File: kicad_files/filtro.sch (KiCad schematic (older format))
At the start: 16 parts

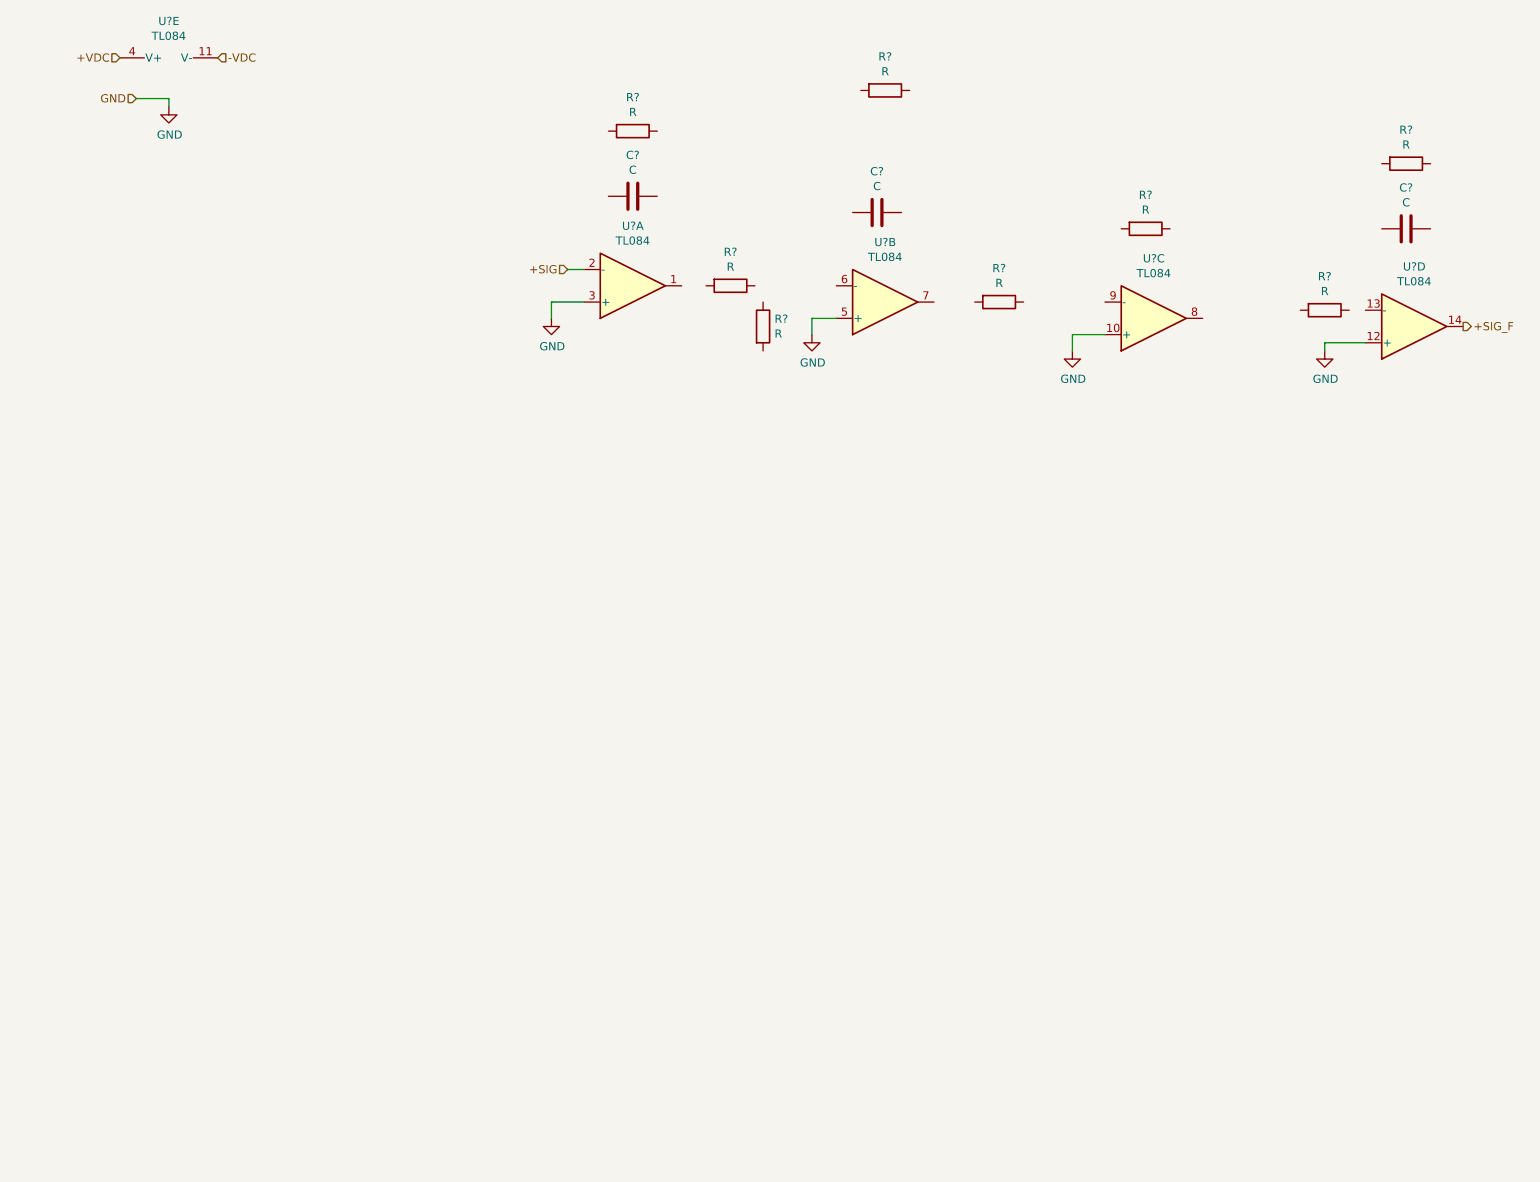
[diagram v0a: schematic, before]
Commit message: Esquemático do filtro conectado e revisado
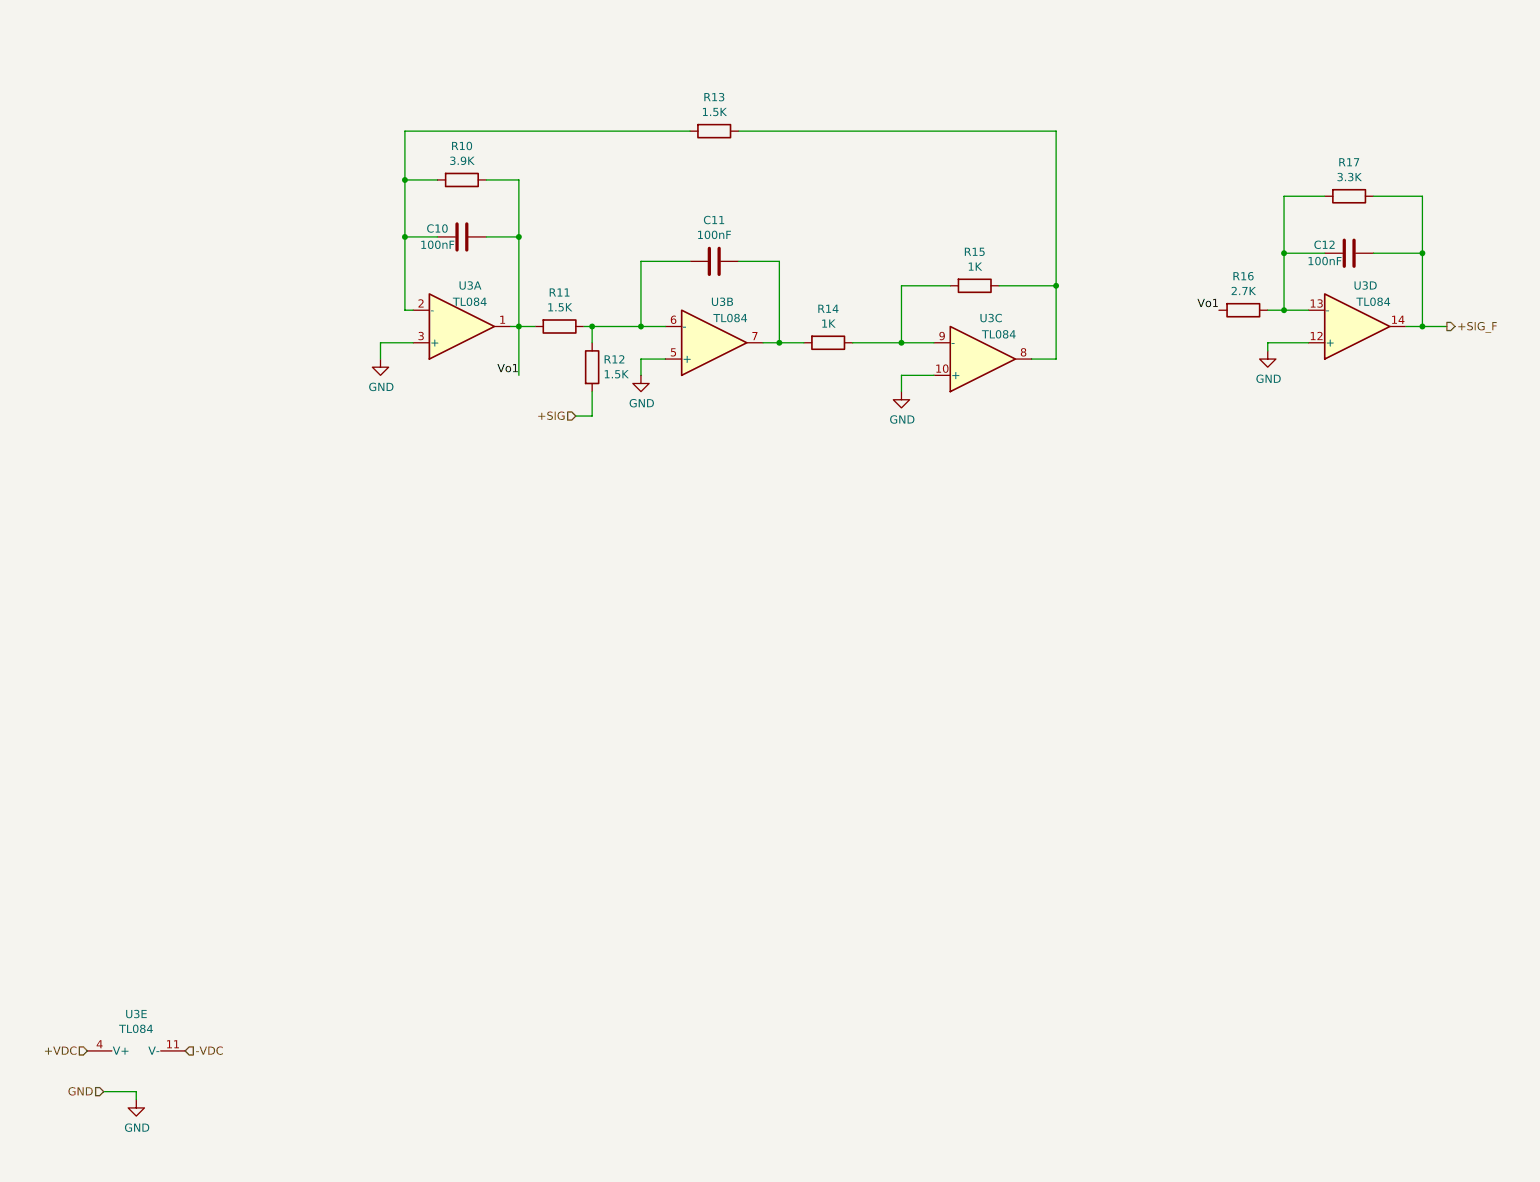
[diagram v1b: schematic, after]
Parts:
- C10, C11, C12: renamed from C?; value C -> 100nF
- R10: renamed from R?; value R -> 3.9K
- R11, R12, R13: renamed from R?; value R -> 1.5K
- R14, R15: renamed from R?; value R -> 1K
- R16: renamed from R?; value R -> 2.7K
- R17: renamed from R?; value R -> 3.3K
- gave numbers to parts that had none: 1
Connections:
- net +SIG: now also R12.2; no longer U3.2 (-)
- net +SIG_F: now also C12.1, R17.1
- net Vo1: now reaches U3.1
- net Vo1: now also C10.1, R10.1, R11.2, R16.2
- net at U3.6 (-): now also C11.2, R11.1, R12.1
- net at U3.7: now also C11.1, R14.2
- net at U3.8: now also R13.1, R15.1
- net at U3.9 (-): now also R14.1, R15.2
- net at U3.13 (-): now also C12.2, R16.1, R17.2
- net at C10.2: now also R10.2, R13.2, U3.2 (-)
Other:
- moved on the sheet: C10, C11, C12, R10, R11, R12, R13, R14, R15, R16, R17, U3A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

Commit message: Adicionados comentários e PDF gerado
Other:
- note added: "Alimentação"
- note added: "Primeiro estágio - Filtro de segunda ordem"
- note added: "Segundo estágio - Filtro de primeira ordem"
- moved on the sheet: C10, C11, C12, R10, R11, R12, R13, R14, R15, R16, R17, U3A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

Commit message: Adicionados footprints aos componentes
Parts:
- C10, C11, C12: footprint (none) -> Capacitor_THT:C_Disc_D4.7mm_W2.5mm_P5.00mm
- R10, R11, R12, R13, R14, R15, R16, R17: footprint (none) -> Resistor_THT:R_Axial_DIN0207_L6.3mm_D2.5mm_P7.62mm_Horizontal
- U3: footprint (none) -> Package_DIP:DIP-14_W7.62mm_Socket_LongPads
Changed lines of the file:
@@
 F 0 "U3" H 1450 4250 50  0000 C CNN
 F 1 "TL084" H 1450 4350 50  0000 C CNN
-F 2 "" H 1350 4600 50  0001 C CNN
+F 2 "Package_DIP:DIP-14_W7.62mm_Socket_LongPads" H 1350 4600 50  0001 C CNN
 F 3 "http://www.ti.com/lit/ds/symlink/tl081.pdf" H 1450 4700 50  0001 C CNN
 	1    1400 4500
@@
 F 0 "U3" H 3000 4350 50  0000 C CNN
 F 1 "TL084" H 3050 4450 50  0000 C CNN
-F 2 "" H 2900 4700 50  0001 C CNN
+F 2 "Package_DIP:DIP-14_W7.62mm_Socket_LongPads" H 2900 4700 50  0001 C CNN
 F 3 "http://www.ti.com/lit/ds/symlink/tl081.pdf" H 3000 4800 50  0001 C CNN
 	2    2950 4600
@@
 F 0 "U3" H 7150 4150 50  0000 C CNN
 F 1 "TL084" H 7200 4250 50  0000 C CNN
-F 2 "" H 7050 4500 50  0001 C CNN
+F 2 "Package_DIP:DIP-14_W7.62mm_Socket_LongPads" H 7050 4500 50  0001 C CNN
 F 3 "http://www.ti.com/lit/ds/symlink/tl081.pdf" H 7150 4600 50  0001 C CNN
 	4    7100 4400
@@
 F 0 "U3" V 1125 6950 50  0000 C CNN
 F 1 "TL084" V 1216 6950 50  0000 C CNN
-F 2 "" H 1400 7050 50  0001 C CNN
+F 2 "Package_DIP:DIP-14_W7.62mm_Socket_LongPads" H 1400 7050 50  0001 C CNN
 F 3 "http://www.ti.com/lit/ds/symlink/tl081.pdf" H 1500 7150 50  0001 C CNN
 	5    1450 6950
@@
 F 0 "C10" V 1350 3800 50  0000 C CNN
 F 1 "100nF" V 1450 3800 50  0000 C CNN
-F 2 "" H 1438 3800 50  0001 C CNN
+F 2 "Capacitor_THT:C_Disc_D4.7mm_W2.5mm_P5.00mm" H 1438 3800 50  0001 C CNN
 F 3 "~" H 1400 3950 50  0001 C CNN
 	1    1400 3950
@@
 F 0 "C11" V 2698 4100 50  0000 C CNN
 F 1 "100nF" V 2789 4100 50  0000 C CNN
-F 2 "" H 2988 3950 50  0001 C CNN
+F 2 "Capacitor_THT:C_Disc_D4.7mm_W2.5mm_P5.00mm" H 2988 3950 50  0001 C CNN
 F 3 "~" H 2950 4100 50  0001 C CNN
 	1    2950 4100
@@
 F 0 "C12" V 7000 3800 50  0000 C CNN
 F 1 "100nF" V 7100 3800 50  0000 C CNN
-F 2 "" H 7088 3800 50  0001 C CNN
+F 2 "Capacitor_THT:C_Disc_D4.7mm_W2.5mm_P5.00mm" H 7088 3800 50  0001 C CNN
 F 3 "~" H 7050 3950 50  0001 C CNN
 	1    7050 3950
@@
 F 0 "R12" H 2270 4796 50  0000 L CNN
 F 1 "1.5K" H 2270 4705 50  0000 L CNN
-F 2 "" V 2130 4750 50  0001 C CNN
+F 2 "Resistor_THT:R_Axial_DIN0207_L6.3mm_D2.5mm_P7.62mm_Horizontal" V 2130 4750 50  0001 C CNN
 F 3 "~" H 2200 4750 50  0001 C CNN
 	1    2200 4750
@@
 F 0 "R11" V 1793 4500 50  0000 C CNN
 F 1 "1.5K" V 1884 4500 50  0000 C CNN
-F 2 "" V 1930 4500 50  0001 C CNN
+F 2 "Resistor_THT:R_Axial_DIN0207_L6.3mm_D2.5mm_P7.62mm_Horizontal" V 1930 4500 50  0001 C CNN
 F 3 "~" H 2000 4500 50  0001 C CNN
 	1    2000 4500
@@
 F 0 "R10" V 1193 3600 50  0000 C CNN
 F 1 "3.9K" V 1284 3600 50  0000 C CNN
-F 2 "" V 1330 3600 50  0001 C CNN
+F 2 "Resistor_THT:R_Axial_DIN0207_L6.3mm_D2.5mm_P7.62mm_Horizontal" V 1330 3600 50  0001 C CNN
 F 3 "~" H 1400 3600 50  0001 C CNN
 	1    1400 3600
@@
 F 0 "R13" V 2743 3300 50  0000 C CNN
 F 1 "1.5K" V 2834 3300 50  0000 C CNN
-F 2 "" V 2880 3300 50  0001 C CNN
+F 2 "Resistor_THT:R_Axial_DIN0207_L6.3mm_D2.5mm_P7.62mm_Horizontal" V 2880 3300 50  0001 C CNN
 F 3 "~" H 2950 3300 50  0001 C CNN
 	1    2950 3300
@@
 F 0 "R14" V 3443 4600 50  0000 C CNN
 F 1 "1K" V 3534 4600 50  0000 C CNN
-F 2 "" V 3580 4600 50  0001 C CNN
+F 2 "Resistor_THT:R_Axial_DIN0207_L6.3mm_D2.5mm_P7.62mm_Horizontal" V 3580 4600 50  0001 C CNN
 F 3 "~" H 3650 4600 50  0001 C CNN
 	1    3650 4600
@@
 F 0 "R17" V 6843 3600 50  0000 C CNN
 F 1 "3.3K" V 6934 3600 50  0000 C CNN
-F 2 "" V 6980 3600 50  0001 C CNN
+F 2 "Resistor_THT:R_Axial_DIN0207_L6.3mm_D2.5mm_P7.62mm_Horizontal" V 6980 3600 50  0001 C CNN
 F 3 "~" H 7050 3600 50  0001 C CNN
 	1    7050 3600
@@
 F 0 "R15" V 4343 4250 50  0000 C CNN
 F 1 "1K" V 4434 4250 50  0000 C CNN
-F 2 "" V 4480 4250 50  0001 C CNN
+F 2 "Resistor_THT:R_Axial_DIN0207_L6.3mm_D2.5mm_P7.62mm_Horizontal" V 4480 4250 50  0001 C CNN
 F 3 "~" H 4550 4250 50  0001 C CNN
 	1    4550 4250
@@
 F 0 "U3" H 4650 4450 50  0000 C CNN
 F 1 "TL084" H 4700 4550 50  0000 C CNN
-F 2 "" H 4550 4800 50  0001 C CNN
+F 2 "Package_DIP:DIP-14_W7.62mm_Socket_LongPads" H 4550 4800 50  0001 C CNN
 F 3 "http://www.ti.com/lit/ds/symlink/tl081.pdf" H 4650 4900 50  0001 C CNN
 	3    4600 4700
@@
 F 0 "R16" V 6193 4300 50  0000 C CNN
 F 1 "2.7K" V 6284 4300 50  0000 C CNN
-F 2 "" V 6330 4300 50  0001 C CNN
+F 2 "Resistor_THT:R_Axial_DIN0207_L6.3mm_D2.5mm_P7.62mm_Horizontal" V 6330 4300 50  0001 C CNN
 F 3 "~" H 6400 4300 50  0001 C CNN
 	1    6400 4300

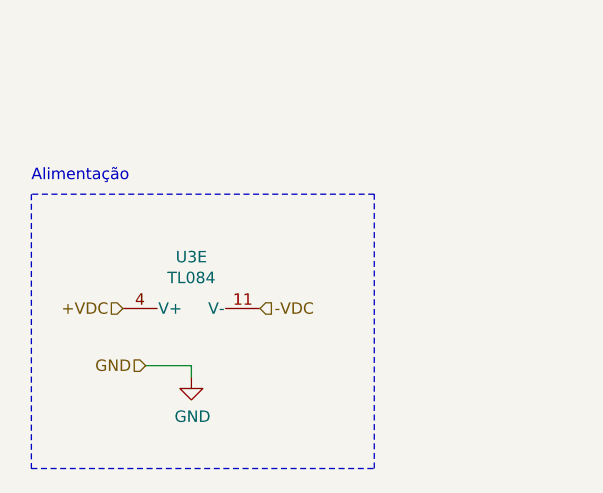
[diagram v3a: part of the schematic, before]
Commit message: Importados componentes no layout PCB e adicionados capacitores de bypass no TL084
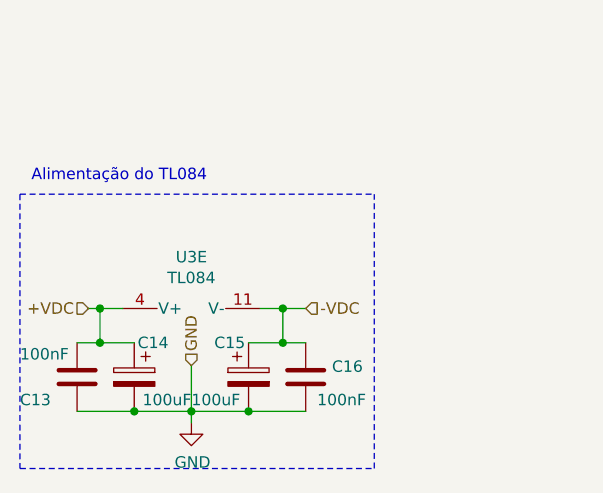
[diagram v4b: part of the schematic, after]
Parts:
- added C13, C16: 100nF, Capacitor_THT:C_Disc_D4.7mm_W2.5mm_P5.00mm, symbol Device:C
- added C14, C15: 100uF, Capacitor_THT:CP_Radial_D5.0mm_P2.50mm, symbol Device:CP
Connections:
- net +VDC: now also C13.1, C14.1
- net -VDC: now also C15.1, C16.1
- net GND: now also C13.2, C14.2, C15.2, C16.2
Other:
- note added: "Alimentação do TL084"
- note removed: "Alimentação"
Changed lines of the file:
@@
 Sheet 2 2
 Title "Amplificador de Áudio"
-Date "2020-06-30"
-Rev "2"
+Date "2020-07-01"
+Rev "3"
 Comp "UFS"
 Comment1 "Design por Raphael Cardoso"
@@
 	0    -1   1    0
 $EndComp
-Text HLabel 1150 6850 0    50   Input ~ 0
+Text HLabel 1000 6850 0    50   Input ~ 0
 +VDC
-Text HLabel 1750 6850 2    50   Input ~ 0
--VDC
-Text HLabel 1250 7100 0    50   Input ~ 0
+Text HLabel 1450 7100 1    50   Input ~ 0
 GND
 $Comp
 L power:GND #PWR01
 U 1 1 5F0E079D
-P 1450 7150
-F 0 "#PWR01" H 1450 6900 50  0001 C CNN
-F 1 "GND" H 1455 6977 50  0000 C CNN
-F 2 "" H 1450 7150 50  0001 C CNN
-F 3 "" H 1450 7150 50  0001 C CNN
-	1    1450 7150
-	1    0    0    -1
-$EndComp
-Wire Wire Line
-	1250 7100 1450 7100
-Wire Wire Line
-	1450 7100 1450 7150
+P 1450 7350
+F 0 "#PWR01" H 1450 7100 50  0001 C CNN
+F 1 "GND" H 1455 7177 50  0000 C CNN
+F 2 "" H 1450 7350 50  0001 C CNN
+F 3 "" H 1450 7350 50  0001 C CNN
+	1    1450 7350
+	1    0    0    -1
+$EndComp
+Wire Wire Line
+	1450 7100 1450 7300
 $Comp
 L power:GND #PWR02
@@
 Segundo estágio - Filtro de primeira ordem
 Wire Notes Line
-	750  6350 750  7550
-Wire Notes Line
-	750  7550 2250 7550
+	700  6350 700  7550
 Wire Notes Line
 	2250 7550 2250 6350
-Wire Notes Line
-	2250 6350 750  6350
 Text Notes 750  6300 0    50   ~ 0
-Alimentação
+Alimentação do TL084
+$Comp
+L Device:C C16
+U 1 1 5EFD5E63
+P 1950 7150
+F 0 "C16" H 2065 7196 50  0000 L CNN
+F 1 "100nF" H 2000 7050 50  0000 L CNN
+F 2 "Capacitor_THT:C_Disc_D4.7mm_W2.5mm_P5.00mm" H 1988 7000 50  0001 C CNN
+F 3 "~" H 1950 7150 50  0001 C CNN
+	1    1950 7150
+	1    0    0    -1
+$EndComp
+Text HLabel 1950 6850 2    50   Input ~ 0
+-VDC
+Wire Wire Line
+	1850 6850 1750 6850
+Wire Wire Line
+	1950 6850 1850 6850
+Connection ~ 1850 6850
+Wire Notes Line
+	700  6350 2250 6350
+Wire Notes Line
+	700  7550 2250 7550
+$Comp
+L Device:CP C15
+U 1 1 5EFE7556
+P 1700 7150
+F 0 "C15" H 1550 7300 50  0000 L CNN
+F 1 "100uF" H 1450 7050 50  0000 L CNN
+F 2 "Capacitor_THT:CP_Radial_D5.0mm_P2.50mm" H 1738 7000 50  0001 C CNN
+F 3 "~" H 1700 7150 50  0001 C CNN
+	1    1700 7150
+	1    0    0    -1
+$EndComp
+Wire Wire Line
+	1850 7000 1700 7000
+Wire Wire Line
+	1850 6850 1850 7000
+Wire Wire Line
+	1850 7000 1950 7000
+Connection ~ 1850 7000
+Wire Wire Line
+	1950 7300 1700 7300
+Wire Wire Line
+	1700 7300 1450 7300
+Connection ~ 1700 7300
+Connection ~ 1450 7300
+Wire Wire Line
+	1450 7300 1450 7350
+$Comp
+L Device:CP C14
+U 1 1 5EFEF689
+P 1200 7150
+F 0 "C14" H 1050 7300 50  0000 L CNN
+F 1 "100uF" H 950 7050 50  0000 L CNN
+F 2 "Capacitor_THT:CP_Radial_D5.0mm_P2.50mm" H 1238 7000 50  0001 C CNN
+F 3 "~" H 1200 7150 50  0001 C CNN
+	1    1200 7150
+	-1   0    0    -1
+$EndComp
+$Comp
+L Device:C C13
+U 1 1 5EFF003F
+P 950 7150
+F 0 "C13" H 700 7050 50  0000 L CNN
+F 1 "100nF" H 700 7250 50  0000 L CNN
+F 2 "Capacitor_THT:C_Disc_D4.7mm_W2.5mm_P5.00mm" H 988 7000 50  0001 C CNN
+F 3 "~" H 950 7150 50  0001 C CNN
+	1    950  7150
+	1    0    0    -1
+$EndComp
+Wire Wire Line
+	950  7300 1200 7300
+Wire Wire Line
+	1200 7300 1450 7300
+Connection ~ 1200 7300
+Wire Wire Line
+	1000 6850 1050 6850
+Wire Wire Line
+	950  7000 1050 7000
+Wire Wire Line
+	1050 6850 1050 7000
+Connection ~ 1050 6850
+Wire Wire Line
+	1050 6850 1150 6850
+Connection ~ 1050 7000
+Wire Wire Line
+	1050 7000 1200 7000
 $EndSCHEMATC
